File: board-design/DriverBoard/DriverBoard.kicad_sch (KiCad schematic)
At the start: 0 parts

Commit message: updated board schematic - NEEED TO ADD GITIGNORE
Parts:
- added C1, C2: C, symbol Device:C
- added R1, R2: R, symbol Device:R
- added U1, U4: LM393, symbol Comparator:LM393
- added U2: 74HC00, symbol 74xx:74HC00
- added U3, U5: LMC6482, symbol Amplifier_Operational:LMC6482
- added U6: 74LS174, symbol 74xx:74LS174
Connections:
- new net: C1.1, R1.2, U1.1
- new net: C2.1, R2.2, U4.1
- new net GND: C1.2, C2.2

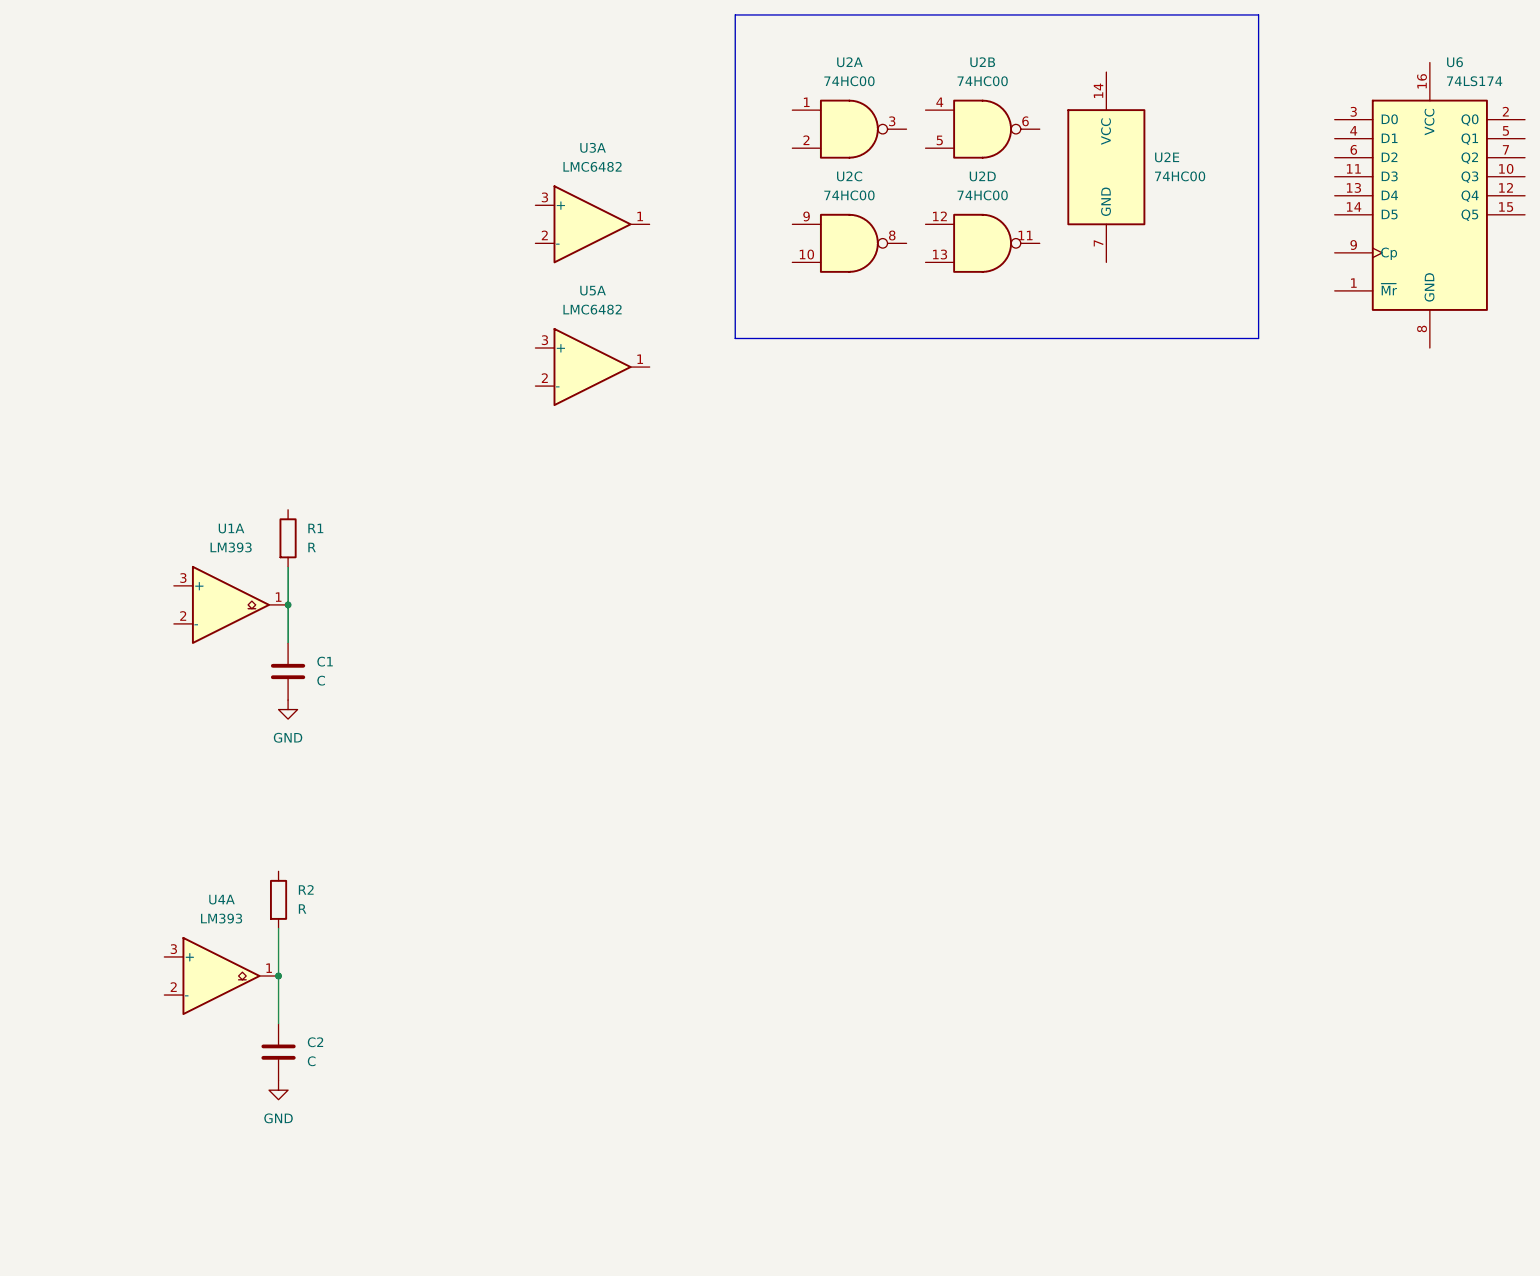
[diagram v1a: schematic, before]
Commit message: correctly add U1, U3, U4 and U5
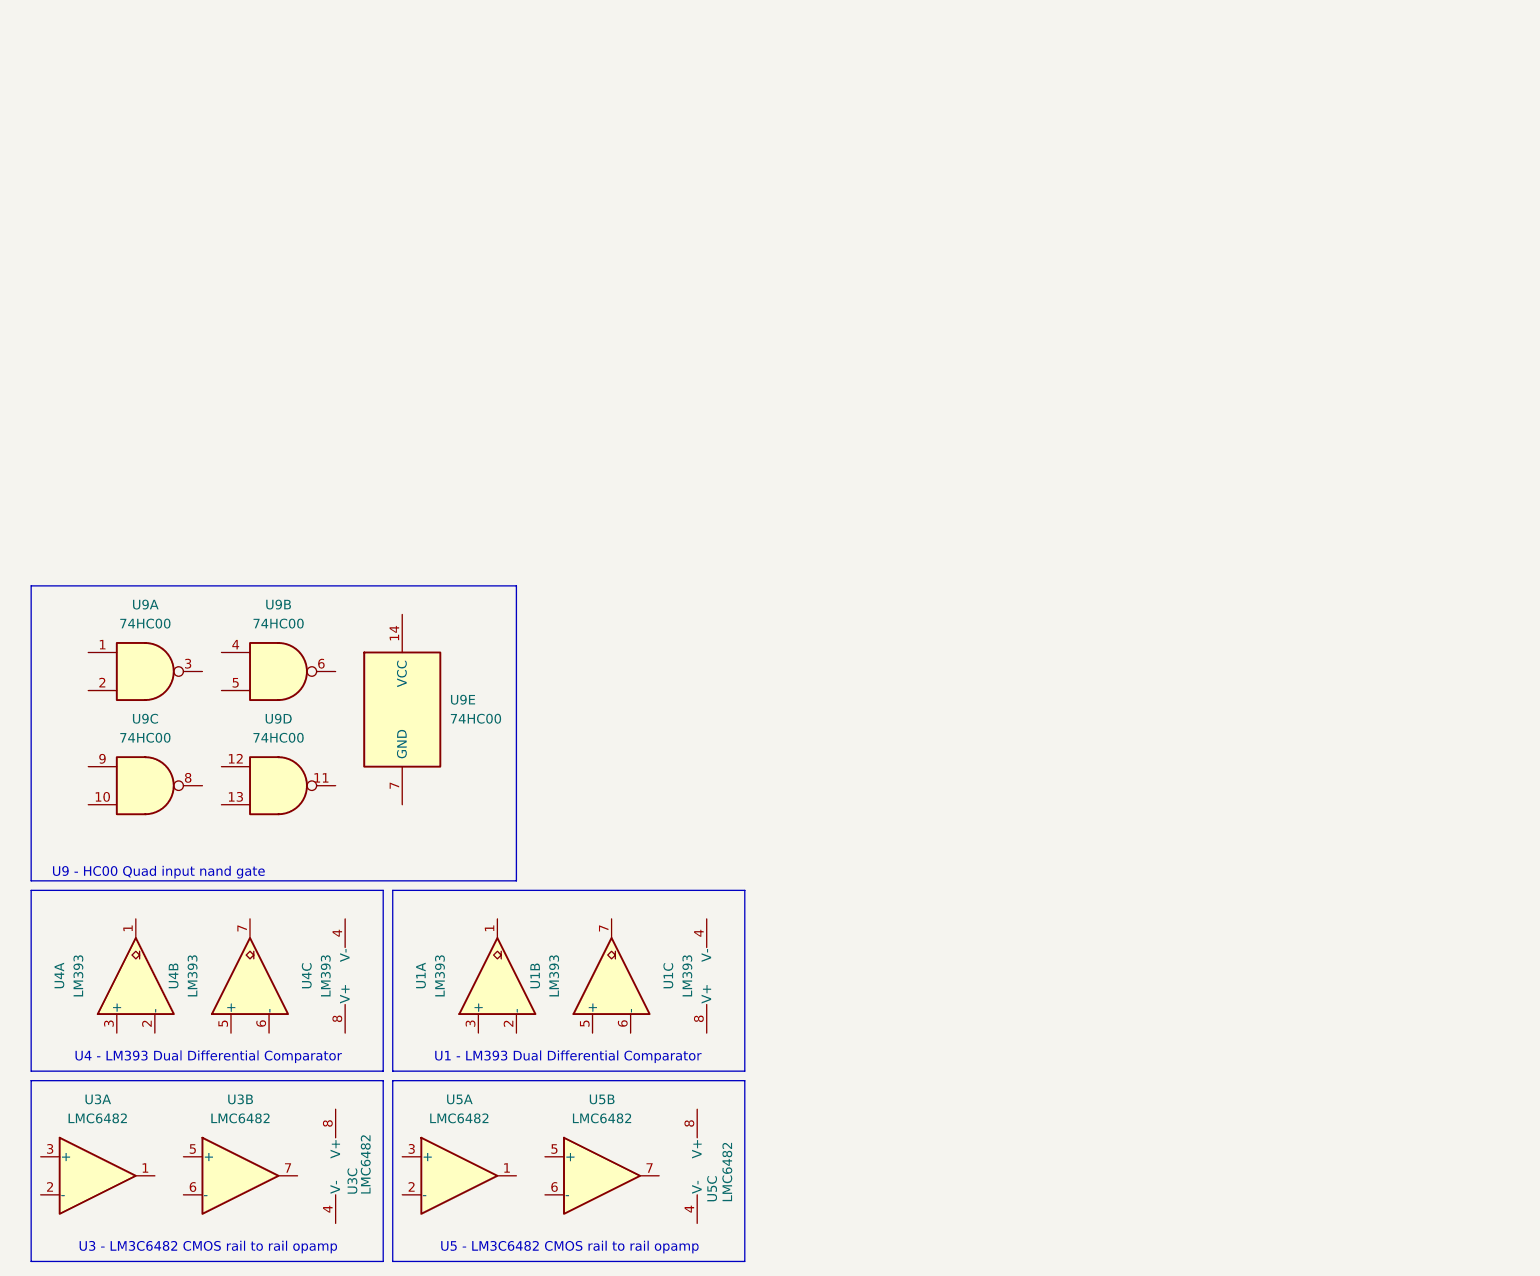
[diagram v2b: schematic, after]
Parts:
- removed C1, C2: C, symbol Device:C
- removed R1, R2: R, symbol Device:R
- removed U6: 74LS174, symbol 74xx:74LS174
- added unit 2 of U1
- added unit 3 of U1
- added unit 2 of U3
- added unit 3 of U3
- added unit 2 of U4
- added unit 3 of U4
- added unit 3 of U5
- added unit 2 of U5
- renumbered U2 to U9
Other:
- note added: "U1 - LM393 Dual Differential Comparator"
- note added: "U3 - LM3C6482 CMOS rail to rail opamp"
- note added: "U4 - LM393 Dual Differential Comparator"
- note added: "U5 - LM3C6482 CMOS rail to rail opamp"
- note added: "U9 - HC00 Quad input nand gate"
- moved on the sheet: U9A, U9B, U9C, U9D, U9E

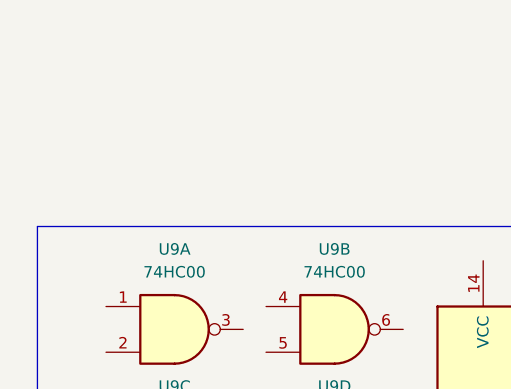
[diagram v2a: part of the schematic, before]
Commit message: update design with power resistors and add sheet comments
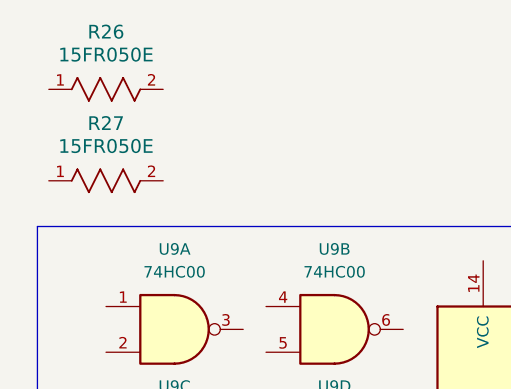
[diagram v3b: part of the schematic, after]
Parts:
- added R26, R27: 15FR050E, RES_15_OHM, symbol 2025-09-28_04-50-52:15FR050E
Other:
- company: (none) -> FERMILAB - PARKER LANDON & EM V
- title: (none) -> Driver Board Reverse Engineering
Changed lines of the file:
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@@
 	(generator_version "9.0")
 	(paper "A4")
+	(title_block
+		(title "Driver Board Reverse Engineering")
+		(date "2025-09-28")
+		(rev "1")
+		(company "FERMILAB - PARKER LANDON & EM V")
+		(comment 1 "PCB: 1003598 Nov. 2009 V2")
+		(comment 2 "Reverse engineering a board made by Calmar Laser Inc.")
+	)
 	(rectangle
 		(start 16.51 144.78)
@@
 	)
 	(symbol
+		(lib_id "2025-09-28_04-50-52:15FR050E")
+		(at 17.78 99.06 0)
+		(unit 1)
+		(exclude_from_sim no)
+		(in_bom yes)
+		(on_board yes)
+		(dnp no)
+		(fields_autoplaced yes)
+		(property "Reference" "R27"
+			(at 24.13 92.71 0)
+			(effects
+				(font
+					(size 1.524 1.524)
+				)
+			)
+		)
+		(property "Value" "15FR050E"
+			(at 24.13 95.25 0)
+			(effects
+				(font
+					(size 1.524 1.524)
+				)
+			)
+		)
+		(property "Footprint" "RES_15_OHM"
+			(at 17.78 99.06 0)
+			(effects
+				(font
+					(size 1.27 1.27)
+					(italic yes)
+				)
+				(hide yes)
+			)
+		)
+		(property "Datasheet" "15FR050E"
+			(at 17.78 99.06 0)
+			(effects
+				(font
+					(size 1.27 1.27)
+					(italic yes)
+				)
+				(hide yes)
+			)
+		)
+		(property "Description" ""
+			(at 17.78 99.06 0)
+			(effects
+				(font
+					(size 1.27 1.27)
+				)
+				(hide yes)
+			)
+		)
+		(pin "1"
+		)
+		(pin "2"
+		)
+		(instances
+			(project ""
+				(path "/4cdfe5ad-52c6-4407-9638-f2feb0b16a90"
+					(reference "R27")
+					(unit 1)
+				)
+			)
+		)
+	)
+	(symbol
 		(lib_id "Comparator:LM393")
 		(at 45.72 156.21 90)
@@
 					(unit 1)
 				)
+			)
+		)
+	)
+	(symbol
+		(lib_id "2025-09-28_04-50-52:15FR050E")
+		(at 17.78 88.9 0)
+		(unit 1)
+		(exclude_from_sim no)
+		(in_bom yes)
+		(on_board yes)
+		(dnp no)
+		(fields_autoplaced yes)
+		(property "Reference" "R26"
+			(at 24.13 82.55 0)
+			(effects
+				(font
+					(size 1.524 1.524)
+				)
+			)
+		)
+		(property "Value" "15FR050E"
+			(at 24.13 85.09 0)
+			(effects
+				(font
+					(size 1.524 1.524)
+				)
+			)
+		)
+		(property "Footprint" "RES_15_OHM"
+			(at 17.78 88.9 0)
+			(effects
+				(font
+					(size 1.27 1.27)
+					(italic yes)
+				)
+				(hide yes)
+			)
+		)
+		(property "Datasheet" "15FR050E"
+			(at 17.78 88.9 0)
+			(effects
+				(font
+					(size 1.27 1.27)
+					(italic yes)
+				)
+				(hide yes)
+			)
+		)
+		(property "Description" ""
+			(at 17.78 88.9 0)
+			(effects
+				(font
+					(size 1.27 1.27)
+				)
+				(hide yes)
+			)
+		)
+		(pin "1"
+		)
+		(pin "2"
+		)
+		(instances
+			(project ""
+				(path "/4cdfe5ad-52c6-4407-9638-f2feb0b16a90"
+					(reference "R26")
+					(unit 1)
+				)

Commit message: add some backside components to the sheet, and create a TEC5V6A symbol
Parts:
- added D4, D5, D6, D7: MBR60100CT, Package_TO_SOT_THT:TO-220-3_Vertical, symbol Diode:MBR745
- added Q1: IRL3302, Package_TO_SOT_THT:TO-220-3_Vertical, symbol Transistor_FET:IRF3205
- added U10: 74AUC2G79, symbol 74xGxx:74AUC2G79
- added U11: SN74LVC1G332, symbol 74xGxx:74LVC1G332
- added U7: ~, symbol LaserDriverComponents:TEC5V6AD
